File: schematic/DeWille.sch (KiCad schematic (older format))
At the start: 0 parts

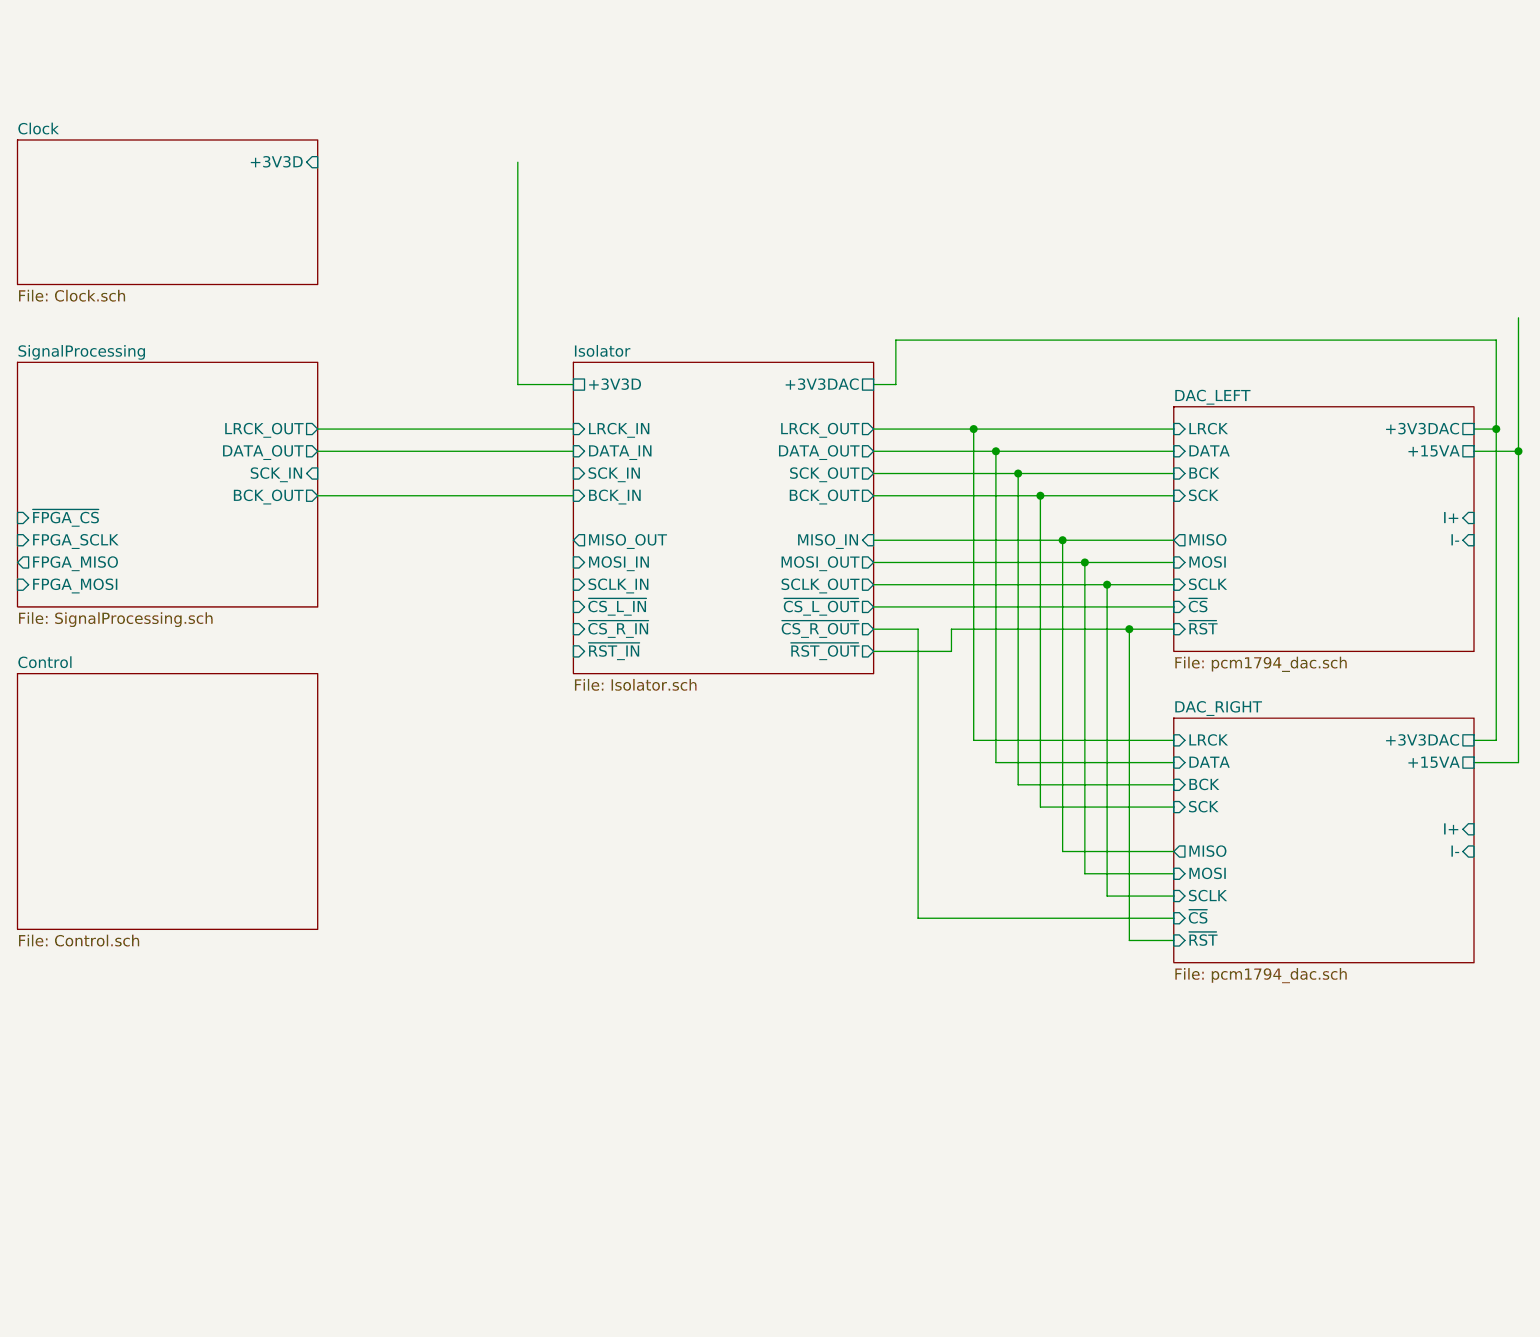
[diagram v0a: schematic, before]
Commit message: Clock generation mostly complete. Some inter-module connections fixed.
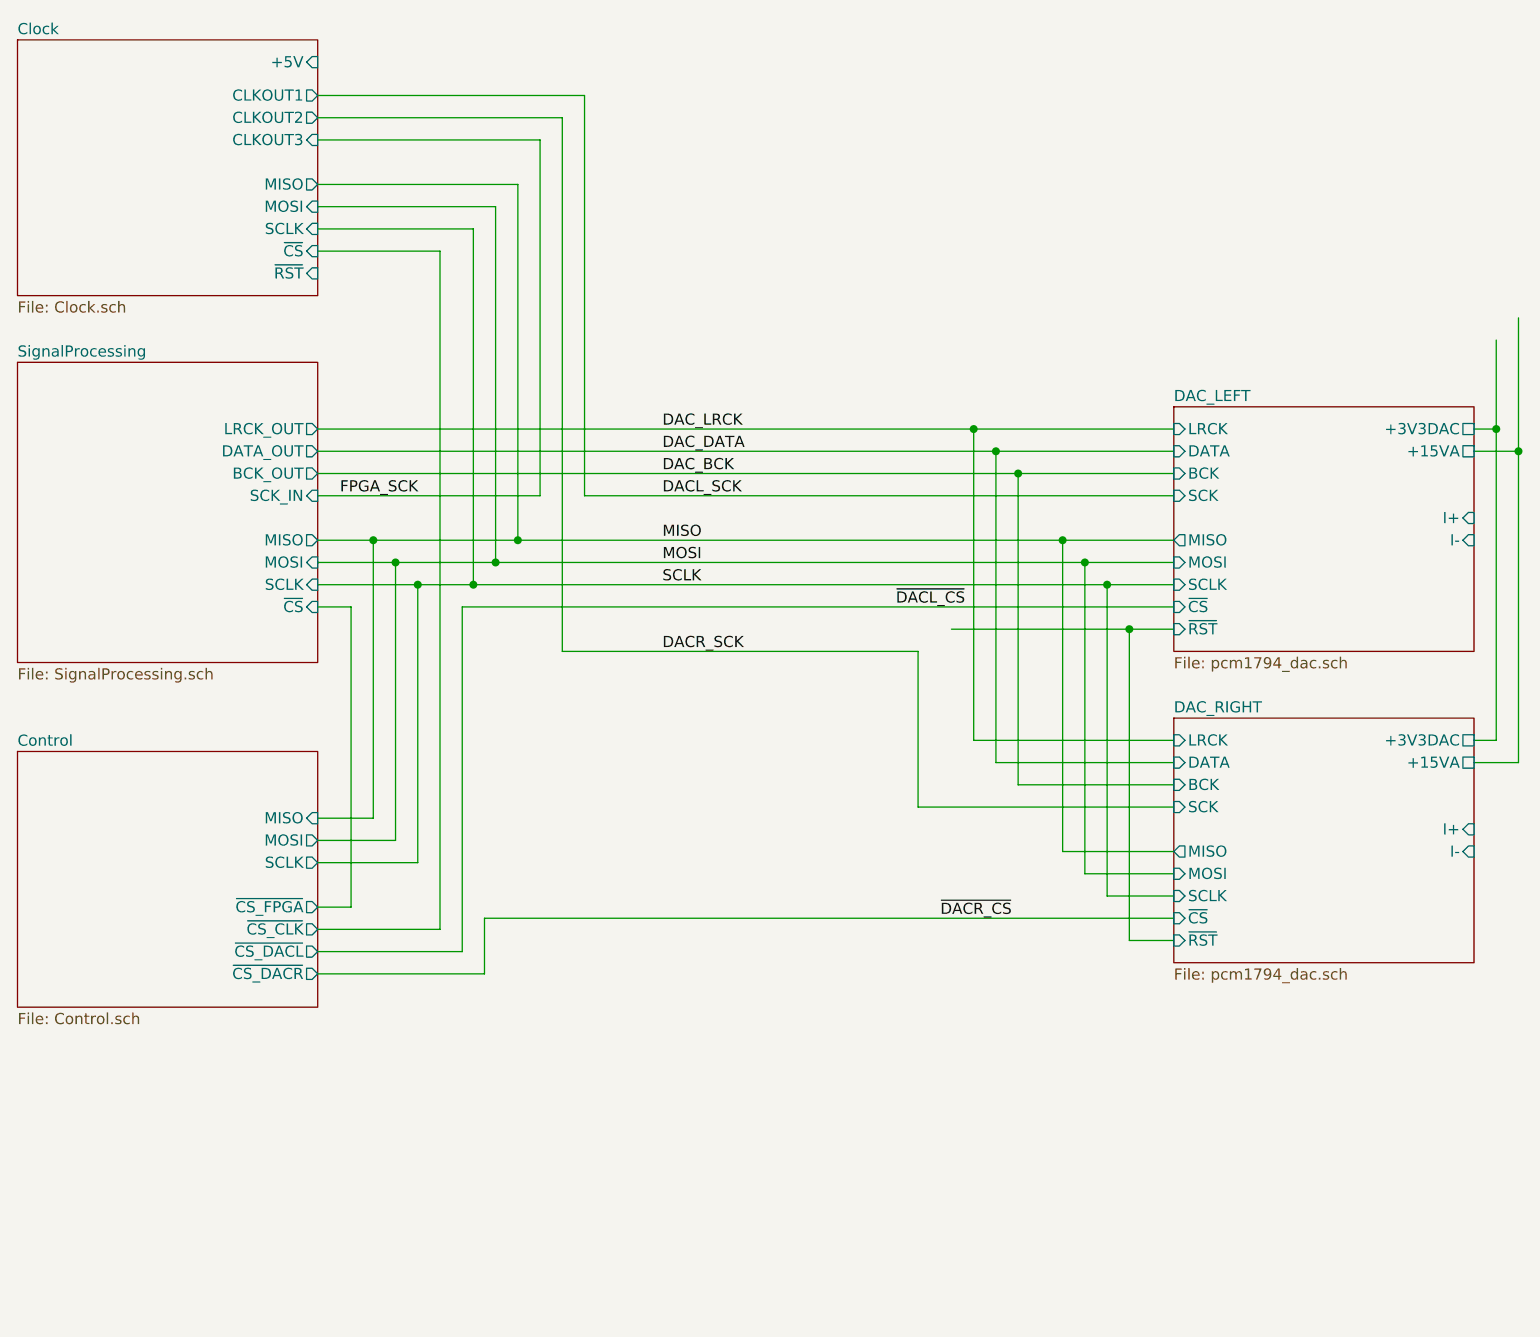
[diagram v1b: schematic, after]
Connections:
- net labels added: DACL_SCK, DACR_SCK, DAC_BCK, DAC_DATA, DAC_LRCK, FPGA_SCK, MISO, MOSI, SCLK, ~DACL_CS~, ~DACR_CS~
- wire segments 54 -> 77
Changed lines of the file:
@@
 $Descr A3 16535 11693
 encoding utf-8
-Sheet 1 7
+Sheet 1 6
 Title "DeWille"
 Date "2019-11-01"
@@
 	10500 5500 11200 5500
 Wire Wire Line
-	11200 5600 10600 5600
-Wire Wire Line
-	10600 5600 10600 4200
-Wire Wire Line
-	10600 4200 11200 4200
-Wire Wire Line
 	11200 4400 10700 4400
 Wire Wire Line
@@
 Wire Wire Line
 	11000 4800 11200 4800
-Wire Wire Line
-	10300 3900 9850 3900
 Connection ~ 10300 3900
-Wire Wire Line
-	10400 4000 9850 4000
 Connection ~ 10400 4000
-Wire Wire Line
-	9850 4100 10500 4100
-Connection ~ 10500 4100
-Wire Wire Line
-	10600 4200 9850 4200
-Connection ~ 10600 4200
-Wire Wire Line
-	9850 4400 10700 4400
 Connection ~ 10700 4400
-Wire Wire Line
-	10800 4500 9850 4500
 Connection ~ 10800 4500
-Wire Wire Line
-	10900 4600 9850 4600
 Connection ~ 10900 4600
-Wire Wire Line
-	9850 4700 11200 4700
-Wire Wire Line
-	9850 4900 10200 4900
-Wire Wire Line
-	10200 4900 10200 4800
 Wire Wire Line
 	10200 4800 11000 4800
 Connection ~ 11000 4800
 Wire Wire Line
-	10050 6100 10050 4800
-Wire Wire Line
-	10050 4800 9850 4800
-Wire Wire Line
-	10050 6100 11200 6100
-$Sheet
-S 8500 3600 1350 1400
-U 5DCC37DA
-F0 "Isolator" 50
-F1 "Isolator.sch" 50
-F2 "LRCK_OUT" O R 9850 3900 50
-F3 "DATA_OUT" O R 9850 4000 50
-F4 "SCK_OUT" O R 9850 4100 50
-F5 "BCK_OUT" O R 9850 4200 50
-F6 "MOSI_OUT" O R 9850 4500 50
-F7 "SCLK_OUT" O R 9850 4600 50
-F8 "MISO_IN" I R 9850 4400 50
-F9 "~RST_OUT~" O R 9850 4900 50
-F10 "~CS_L_OUT~" O R 9850 4700 50
-F11 "~CS_R_OUT~" O R 9850 4800 50
-F12 "LRCK_IN" I L 8500 3900 50
-F13 "DATA_IN" I L 8500 4000 50
-F14 "BCK_IN" I L 8500 4200 50
-F15 "SCK_IN" I L 8500 4100 50
-F16 "MOSI_IN" I L 8500 4500 50
-F17 "SCLK_IN" I L 8500 4600 50
-F18 "~RST_IN~" I L 8500 4900 50
-F19 "MISO_OUT" O L 8500 4400 50
-F20 "~CS_L_IN~" I L 8500 4700 50
-F21 "~CS_R_IN~" I L 8500 4800 50
-F22 "+3V3DAC" U R 9850 3700 50
-F23 "+3V3D" U L 8500 3700 50
-$EndSheet
-Wire Wire Line
 	12550 3900 12650 3900
 Wire Wire Line
 	12650 3900 12650 3500
-Wire Wire Line
-	12650 3500 9950 3500
-Wire Wire Line
-	9950 3500 9950 3700
-Wire Wire Line
-	9850 3700 9950 3700
-$Sheet
-S 6000 3600 1350 1100
-U 5DCFEDFC
-F0 "SignalProcessing" 50
-F1 "SignalProcessing.sch" 50
-F2 "FPGA_MOSI" I L 6000 4600 50
-F3 "FPGA_MISO" O L 6000 4500 50
-F4 "FPGA_SCLK" I L 6000 4400 50
-F5 "~FPGA_CS~" I L 6000 4300 50
-F6 "LRCK_OUT" O R 7350 3900 50
-F7 "BCK_OUT" O R 7350 4200 50
-F8 "DATA_OUT" O R 7350 4000 50
-F9 "SCK_IN" I R 7350 4100 50
-$EndSheet
 $Sheet
 S 11200 5200 1350 1100
@@
 	12750 4000 12750 5400
 $Sheet
-S 6000 5000 1350 1150
+S 6000 5350 1350 1150
 U 5DDEE9E3
 F0 "Control" 50
 F1 "Control.sch" 50
-$EndSheet
-$Sheet
-S 6000 2600 1350 650
+F2 "MISO" I R 7350 5650 50
+F3 "MOSI" O R 7350 5750 50
+F4 "SCLK" O R 7350 5850 50
+F5 "~CS_DACL~" O R 7350 6250 50
+F6 "~CS_DACR~" O R 7350 6350 50
+F7 "~CS_FPGA~" O R 7350 6050 50
+F8 "~CS_CLK~" O R 7350 6150 50
+$EndSheet
+$Sheet
+S 6000 2150 1350 1150
 U 5DD2C0D9
 F0 "Clock" 50
 F1 "Clock.sch" 50
-F2 "+3V3D" I R 7350 2700 50
-$EndSheet
-Wire Wire Line
-	8250 2700 8250 3700
-Wire Wire Line
-	8250 3700 8500 3700
-Wire Wire Line
-	7350 4000 8500 4000
-Wire Wire Line
-	8500 3900 7350 3900
-Wire Wire Line
-	7350 4200 8500 4200
+F2 "CLKOUT1" O R 7350 2400 50
+F3 "CLKOUT2" O R 7350 2500 50
+F4 "~RST~" I R 7350 3200 50
+F5 "~CS~" I R 7350 3100 50
+F6 "MISO" O R 7350 2800 50
+F7 "SCLK" I R 7350 3000 50
+F8 "MOSI" I R 7350 2900 50
+F9 "+5V" I R 7350 2250 50
+F10 "CLKOUT3" I R 7350 2600 50
+$EndSheet
+Wire Wire Line
+	7350 3900 10300 3900
+Wire Wire Line
+	7350 4000 10400 4000
+$Sheet
+S 6000 3600 1350 1350
+U 5DCFEDFC
+F0 "SignalProcessing" 50
+F1 "SignalProcessing.sch" 50
+F2 "LRCK_OUT" O R 7350 3900 50
+F3 "BCK_OUT" O R 7350 4100 50
+F4 "DATA_OUT" O R 7350 4000 50
+F5 "SCK_IN" I R 7350 4200 50
+F6 "MOSI" I R 7350 4500 50
+F7 "MISO" O R 7350 4400 50
+F8 "SCLK" I R 7350 4600 50
+F9 "~CS~" I R 7350 4700 50
+$EndSheet
+Wire Wire Line
+	7350 4400 7600 4400
+Wire Wire Line
+	7350 4500 7700 4500
+Wire Wire Line
+	7350 4600 7800 4600
+Text Label 8900 4400 0    50   ~ 0
+MISO
+Text Label 8900 4500 0    50   ~ 0
+MOSI
+Text Label 8900 4600 0    50   ~ 0
+SCLK
+Connection ~ 8050 4600
+Wire Wire Line
+	8050 4600 10900 4600
+Wire Wire Line
+	7350 3000 8050 3000
+Wire Wire Line
+	8050 3000 8050 4600
+Wire Wire Line
+	7350 2900 8150 2900
+Wire Wire Line
+	8150 2900 8150 4500
+Connection ~ 8150 4500
+Wire Wire Line
+	8150 4500 10800 4500
+Wire Wire Line
+	7350 2800 8250 2800
+Wire Wire Line
+	8250 2800 8250 4400
+Connection ~ 8250 4400
+Wire Wire Line
+	8250 4400 10700 4400
+Wire Wire Line
+	7350 2600 8350 2600
+Wire Wire Line
+	7350 2500 8450 2500
+Wire Wire Line
+	7350 4100 10500 4100
+Connection ~ 10500 4100
+Wire Wire Line
+	7350 4200 8350 4200
+Wire Wire Line
+	8350 4200 8350 2600
+Wire Wire Line
+	8450 2500 8450 4900
+Wire Wire Line
+	8450 4900 10050 4900
+Wire Wire Line
+	10050 4900 10050 5600
+Wire Wire Line
+	10050 5600 11200 5600
+Wire Wire Line
+	11200 4200 8550 4200
+Wire Wire Line
+	8550 4200 8550 2400
+Wire Wire Line
+	8550 2400 7350 2400
+Text Label 9950 4700 0    50   ~ 0
+~DACL_CS~
+Text Label 10150 6100 0    50   ~ 0
+~DACR_CS~
+Wire Wire Line
+	7600 4400 7600 5650
+Wire Wire Line
+	7600 5650 7350 5650
+Connection ~ 7600 4400
+Wire Wire Line
+	7600 4400 8250 4400
+Wire Wire Line
+	7700 4500 7700 5750
+Wire Wire Line
+	7700 5750 7350 5750
+Connection ~ 7700 4500
+Wire Wire Line
+	7700 4500 8150 4500
+Wire Wire Line
+	7800 4600 7800 5850
+Wire Wire Line
+	7800 5850 7350 5850
+Connection ~ 7800 4600
+Wire Wire Line
+	7800 4600 8050 4600
+Wire Wire Line
+	7350 4700 7500 4700
+Wire Wire Line
+	7500 4700 7500 6050
+Wire Wire Line
+	7500 6050 7350 6050
+Wire Wire Line
+	7350 3100 7900 3100
+Wire Wire Line
+	7900 3100 7900 6150
+Wire Wire Line
+	7900 6150 7350 6150
+Wire Wire Line
+	7350 6250 8000 6250
+Wire Wire Line
+	8000 6250 8000 4700
+Wire Wire Line
+	8000 4700 11200 4700
+Wire Wire Line
+	8100 6100 8100 6350
+Wire Wire Line
+	8100 6350 7350 6350
+Wire Wire Line
+	8100 6100 11200 6100
+Text Label 8900 3900 0    50   ~ 0
+DAC_LRCK
+Text Label 8900 4000 0    50   ~ 0
+DAC_DATA
+Text Label 8900 4100 0    50   ~ 0
+DAC_BCK
+Text Label 8900 4200 0    50   ~ 0
+DACL_SCK
+Text Label 8900 4900 0    50   ~ 0
+DACR_SCK
+Text Label 7450 4200 0    50   ~ 0
+FPGA_SCK
 $EndSCHEMATC

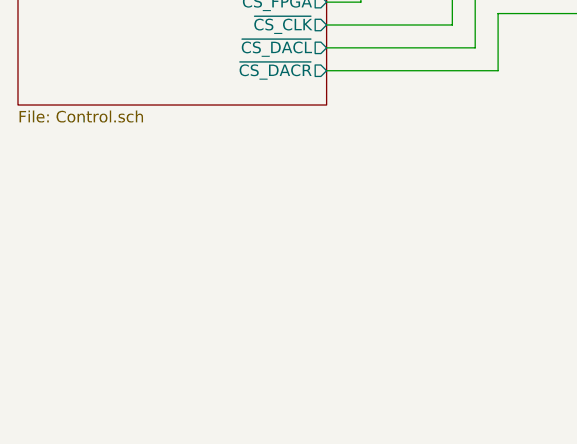
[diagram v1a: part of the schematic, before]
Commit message: Remove galvanic isolator - too much jitter! Add USB interface for Debug and program purposes. Swith to Lattice FPGA
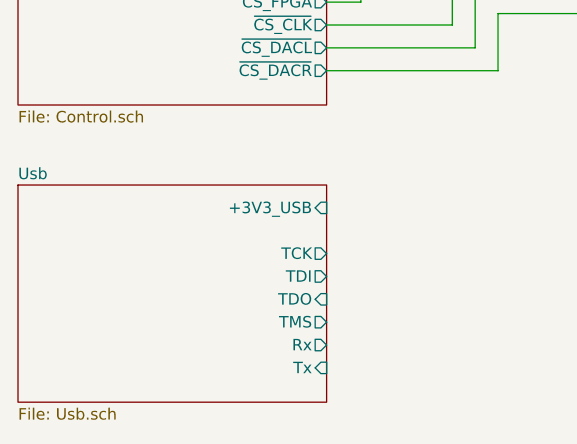
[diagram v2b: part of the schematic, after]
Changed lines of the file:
@@
 $Descr A3 16535 11693
 encoding utf-8
-Sheet 1 6
+Sheet 1 7
 Title "DeWille"
 Date "2019-11-01"
@@
 Text Label 7450 4200 0    50   ~ 0
 FPGA_SCK
+$Sheet
+S 6000 6850 1350 950
+U 5DDC09A7
+F0 "Usb" 50
+F1 "Usb.sch" 50
+F2 "+3V3_USB" I R 7350 6950 50
+F3 "TCK" O R 7350 7150 50
+F4 "TDI" O R 7350 7250 50
+F5 "TDO" I R 7350 7350 50
+F6 "TMS" O R 7350 7450 50
+F7 "Rx" O R 7350 7550 50
+F8 "Tx" I R 7350 7650 50
+$EndSheet
 $EndSCHEMATC
